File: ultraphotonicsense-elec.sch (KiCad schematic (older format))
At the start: 11 parts, among them J1 Conn_SWD_UART, U1 TXB0108PW, U2 74HC164

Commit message: Improved tracks spacing
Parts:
- J1: footprint Connector_JST:JST_PH_B8B-PH-K_1x08_P2.00mm_Vertical -> Connector_JST:JST_XH_B08B-XH-A_1x08_P2.50mm_Vertical
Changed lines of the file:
@@
 F 0 "J1" V 3117 2646 50  0000 C CNN
 F 1 "Conn_SWD_UART" V 3026 2646 50  0000 C CNN
-F 2 "Connector_JST:JST_PH_B8B-PH-K_1x08_P2.00mm_Vertical" H 2900 2700 50  0001 C CNN
+F 2 "Connector_JST:JST_XH_B08B-XH-A_1x08_P2.50mm_Vertical" H 2900 2700 50  0001 C CNN
 F 3 "~" H 2900 2700 50  0001 C CNN
 	1    2900 2700

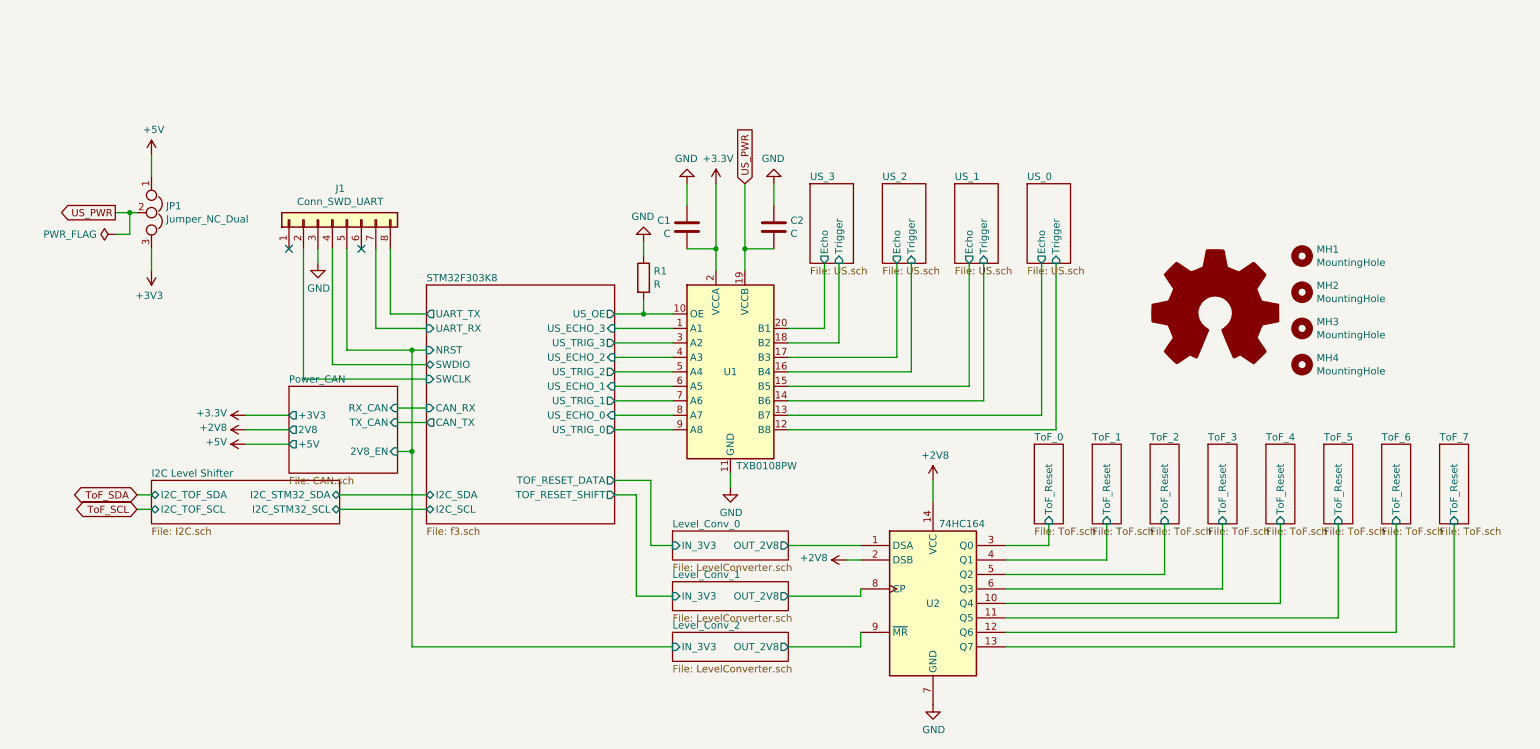
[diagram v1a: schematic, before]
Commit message: Corrected, routing redone
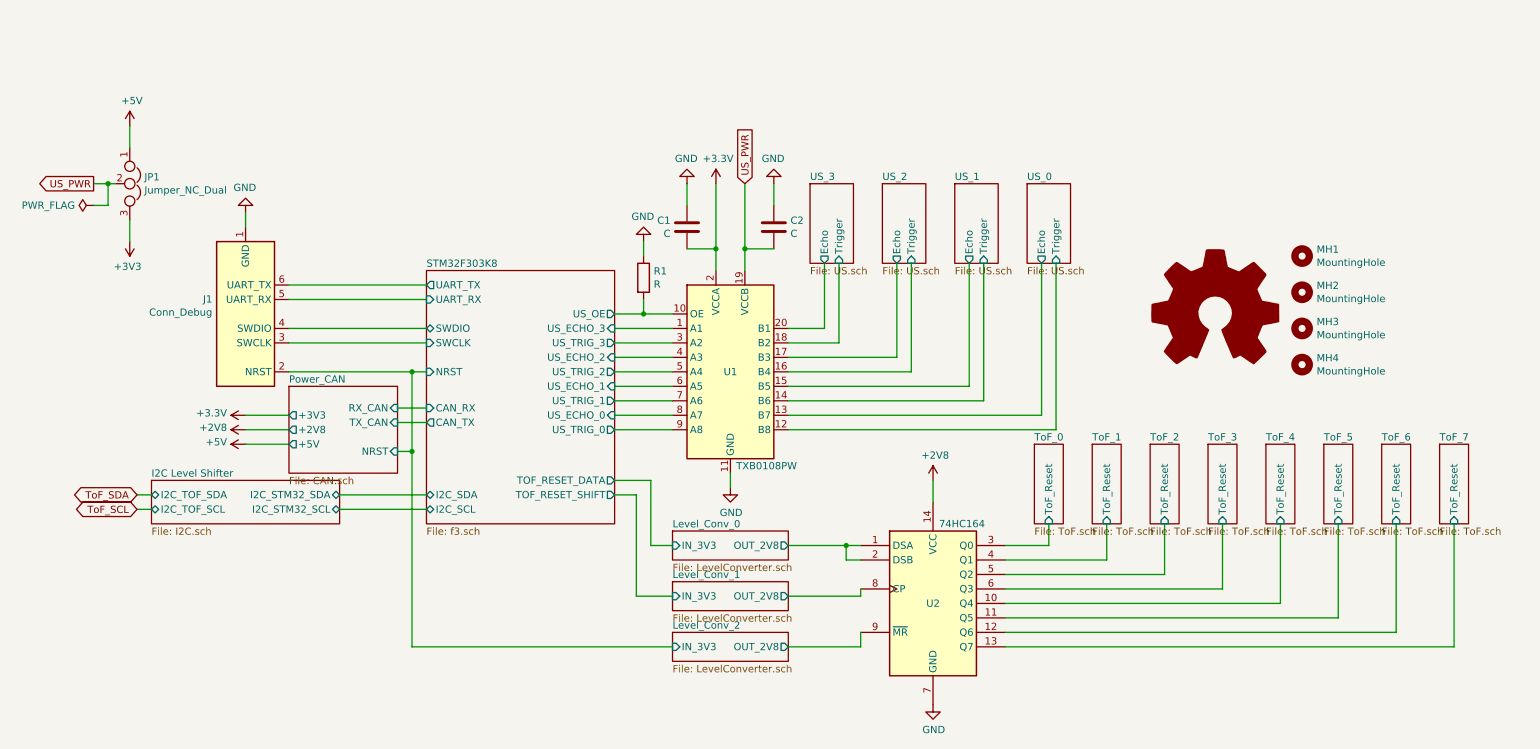
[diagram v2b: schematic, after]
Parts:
- removed J1: Conn_SWD_UART, Connector_JST:JST_XH_B08B-XH-A_1x08_P2.50mm_Vertical, symbol Connector_Generic:Conn_01x08
- added J1: Conn_Debug, Connector_JST:JST_PH_B6B-PH-K_1x06_P2.00mm_Vertical, symbol PhoenixRobotik:Conn_Debug
- U2: RS (none) -> 671-1753
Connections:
- net +2V8: no longer U2.2 (DSB)
- net GND: now also J1.1 (GND)
- net Level_Conv_0/OUT_2V8: now also U2.2 (DSB)
- net Level_Conv_2/IN_3V3: now also J1.2 (NRST)
- net STM32F303K8/SWCLK: now also J1.3 (SWCLK)
- net STM32F303K8/SWDIO: now also J1.4 (SWDIO)
- net STM32F303K8/UART_RX: now also J1.5 (UART_RX)
- net STM32F303K8/UART_TX: now also J1.6 (UART_TX)
- no-connect marks 2 -> 0
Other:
- moved on the sheet: JP1
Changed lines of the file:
@@
 F2 "RX_CAN" I R 3350 4000 50
 F3 "TX_CAN" I R 3350 4100 50
-F4 "2V8_EN" I R 3350 4300 50
-F5 "2V8" O L 2600 4150 50
-F6 "+3V3" O L 2600 4050 50
-F7 "+5V" O L 2600 4250 50
+F5 "+3V3" O L 2600 4050 50
+F6 "+5V" O L 2600 4250 50
+F7 "NRST" I R 3350 4300 50
+F8 "+2V8" O L 2600 4150 50
 $EndSheet
 $Sheet
@@
 $EndComp
 $Comp
-L Connector_Generic:Conn_01x08 J1
-U 1 1 5BBC14EB
-P 2900 2700
-F 0 "J1" V 3117 2646 50  0000 C CNN
-F 1 "Conn_SWD_UART" V 3026 2646 50  0000 C CNN
-F 2 "Connector_JST:JST_XH_B08B-XH-A_1x08_P2.50mm_Vertical" H 2900 2700 50  0001 C CNN
-F 3 "~" H 2900 2700 50  0001 C CNN
-	1    2900 2700
-	0    -1   -1   0
-$EndComp
-Wire Wire Line
-	3300 2900 3300 3350
-Wire Wire Line
-	3300 3350 3550 3350
-Wire Wire Line
-	3200 2900 3200 3450
-Wire Wire Line
-	3200 3450 3550 3450
-NoConn ~ 3100 2900
-Wire Wire Line
-	3000 2900 3000 3600
-Wire Wire Line
-	3000 3600 3450 3600
-Wire Wire Line
-	2900 2900 2900 3700
-Wire Wire Line
-	2900 3700 3550 3700
-$Comp
 L power:GND #PWR07
 U 1 1 5BBC1836
-P 2800 3000
-F 0 "#PWR07" H 2800 2750 50  0001 C CNN
-F 1 "GND" H 2805 2827 50  0000 C CNN
-F 2 "" H 2800 3000 50  0001 C CNN
-F 3 "" H 2800 3000 50  0001 C CNN
-	1    2800 3000
-	1    0    0    -1
-$EndComp
-Wire Wire Line
-	2800 2900 2800 3000
-Wire Wire Line
-	2700 2900 2700 3800
-Wire Wire Line
-	2700 3800 3550 3800
+P 2300 2650
+F 0 "#PWR07" H 2300 2400 50  0001 C CNN
+F 1 "GND" H 2305 2477 50  0000 C CNN
+F 2 "" H 2300 2650 50  0001 C CNN
+F 3 "" H 2300 2650 50  0001 C CNN
+	1    2300 2650
+	-1   0    0    1
+$EndComp
 Wire Wire Line
 	3350 4000 3550 4000
@@
 Wire Wire Line
 	10650 5650 10650 4800
-Wire Wire Line
-	3450 3600 3450 4300
-Wire Wire Line
-	3450 4300 3350 4300
-Connection ~ 3450 3600
-Wire Wire Line
-	3450 3600 3550 3600
 $Comp
 L PhoenixRobotik:74HC164 U2
@@
 F 2 "Package_SO:SOIC-14_3.9x8.7mm_P1.27mm" H 7050 5350 50  0001 C CNN
 F 3 "https://assets.nexperia.com/documents/data-sheet/74HC_HCT164.pdf" H 7050 5350 50  0001 C CNN
+F 4 "671-1753" H 0   0   50  0001 C CNN "RS"
 	1    7050 5350
 	1    0    0    -1
@@
 Wire Wire Line
 	7050 4500 7050 4650
-$Comp
-L power:+2V8 #PWR013
-U 1 1 5BBFB7FF
-P 6450 5050
-F 0 "#PWR013" H 6450 4900 50  0001 C CNN
-F 1 "+2V8" V 6465 5178 50  0000 L CNN
-F 2 "" H 6450 5050 50  0001 C CNN
-F 3 "" H 6450 5050 50  0001 C CNN
-	1    6450 5050
-	0    -1   -1   0
-$EndComp
 Wire Wire Line
 	6450 5050 6550 5050
 $Sheet
-S 3550 3150 1300 1650
+S 3550 3050 1300 1750
 U 5BBD3D7F
 F0 "STM32F303K8" 50
 F1 "f3.sch" 50
-F2 "UART_TX" O L 3550 3350 50
-F3 "UART_RX" I L 3550 3450 50
+F2 "UART_TX" O L 3550 3150 50
+F3 "UART_RX" I L 3550 3250 50
 F4 "CAN_RX" I L 3550 4000 50
 F5 "CAN_TX" O L 3550 4100 50
-F6 "SWDIO" B L 3550 3700 50
-F7 "SWCLK" I L 3550 3800 50
+F6 "SWDIO" B L 3550 3450 50
+F7 "SWCLK" I L 3550 3550 50
 F8 "I2C_SCL" B L 3550 4700 50
 F9 "I2C_SDA" B L 3550 4600 50
-F10 "NRST" I L 3550 3600 50
+F10 "NRST" I L 3550 3750 50
 F11 "TOF_RESET_DATA" O R 4850 4500 50
 F12 "TOF_RESET_SHIFT" O R 4850 4600 50
@@
 $EndSheet
 Wire Wire Line
-	6050 4950 6550 4950
+	6050 4950 6450 4950
 Wire Wire Line
 	5550 2900 5550 3050
@@
 L Device:Jumper_NC_Dual JP1
 U 1 1 5BC62830
-P 1650 2650
-F 0 "JP1" V 1604 2751 50  0000 L CNN
-F 1 "Jumper_NC_Dual" V 1695 2751 50  0000 L CNN
-F 2 "Connector_PinHeader_2.54mm:PinHeader_1x03_P2.54mm_Vertical" H 1650 2650 50  0001 C CNN
-F 3 "~" H 1650 2650 50  0001 C CNN
-	1    1650 2650
+P 1500 2450
+F 0 "JP1" V 1454 2551 50  0000 L CNN
+F 1 "Jumper_NC_Dual" V 1545 2551 50  0000 L CNN
+F 2 "Connector_PinHeader_2.54mm:PinHeader_1x03_P2.54mm_Vertical" H 1500 2450 50  0001 C CNN
+F 3 "~" H 1500 2450 50  0001 C CNN
+	1    1500 2450
 	0    1    1    0
 $EndComp
-Text GLabel 1400 2650 0    50   Output ~ 0
+Text GLabel 1250 2450 0    50   Output ~ 0
 US_PWR
 Wire Wire Line
-	1400 2650 1500 2650
+	1250 2450 1350 2450
 $Comp
 L power:+5V #PWR01
 U 1 1 5BC6506A
-P 1650 2250
-F 0 "#PWR01" H 1650 2100 50  0001 C CNN
-F 1 "+5V" H 1665 2423 50  0000 C CNN
-F 2 "" H 1650 2250 50  0001 C CNN
-F 3 "" H 1650 2250 50  0001 C CNN
-	1    1650 2250
-	1    0    0    -1
-$EndComp
-Wire Wire Line
-	1650 2250 1650 2400
+P 1500 2050
+F 0 "#PWR01" H 1500 1900 50  0001 C CNN
+F 1 "+5V" H 1515 2223 50  0000 C CNN
+F 2 "" H 1500 2050 50  0001 C CNN
+F 3 "" H 1500 2050 50  0001 C CNN
+	1    1500 2050
+	1    0    0    -1
+$EndComp
+Wire Wire Line
+	1500 2050 1500 2200
 $Comp
 L power:+3V3 #PWR02
 U 1 1 5BC678E1
-P 1650 3050
-F 0 "#PWR02" H 1650 2900 50  0001 C CNN
-F 1 "+3V3" H 1665 3223 50  0000 C CNN
-F 2 "" H 1650 3050 50  0001 C CNN
-F 3 "" H 1650 3050 50  0001 C CNN
-	1    1650 3050
+P 1500 2850
+F 0 "#PWR02" H 1500 2700 50  0001 C CNN
+F 1 "+3V3" H 1515 3023 50  0000 C CNN
+F 2 "" H 1500 2850 50  0001 C CNN
+F 3 "" H 1500 2850 50  0001 C CNN
+	1    1500 2850
 	-1   0    0    1
 $EndComp
 Wire Wire Line
-	1650 2900 1650 3050
+	1500 2700 1500 2850
 $Comp
 L power:+3.3V #PWR010
@@
 L power:PWR_FLAG #FLG01
 U 1 1 5BC6A929
-P 1400 2800
-F 0 "#FLG01" H 1400 2875 50  0001 C CNN
-F 1 "PWR_FLAG" V 1400 2928 50  0000 L CNN
-F 2 "" H 1400 2800 50  0001 C CNN
-F 3 "~" H 1400 2800 50  0001 C CNN
-	1    1400 2800
+P 1250 2600
+F 0 "#FLG01" H 1250 2675 50  0001 C CNN
+F 1 "PWR_FLAG" V 1250 2728 50  0000 L CNN
+F 2 "" H 1250 2600 50  0001 C CNN
+F 3 "~" H 1250 2600 50  0001 C CNN
+	1    1250 2600
 	0    -1   -1   0
 $EndComp
 Wire Wire Line
-	1500 2650 1500 2800
-Wire Wire Line
-	1500 2800 1400 2800
-Connection ~ 1500 2650
-Wire Wire Line
-	1500 2650 1550 2650
+	1350 2450 1350 2600
+Wire Wire Line
+	1350 2600 1250 2600
+Connection ~ 1350 2450
+Wire Wire Line
+	1350 2450 1400 2450
 Wire Wire Line
 	5650 4450 5650 4550
@@
 	6800 3000 6800 3650
 Wire Wire Line
+	3450 5650 5250 5650
+Wire Wire Line
+	6050 5650 6550 5650
+Wire Wire Line
+	6550 5650 6550 5550
+Wire Wire Line
+	6550 5300 6550 5250
+Wire Wire Line
+	6050 5300 6550 5300
+Wire Wire Line
+	3350 4300 3450 4300
+Wire Wire Line
 	3450 4300 3450 5650
-Wire Wire Line
-	3450 5650 5250 5650
+$Comp
+L PhoenixRobotik:Conn_Debug J1
+U 1 1 5BD16E64
+P 2300 3350
+F 0 "J1" H 2530 3248 50  0000 L CNN
+F 1 "Conn_Debug" H 2530 3339 50  0000 L CNN
+F 2 "Connector_JST:JST_PH_B6B-PH-K_1x06_P2.00mm_Vertical" H 2700 2050 50  0001 C CNN
+F 3 "~" H 4500 3150 50  0001 C CNN
+	1    2300 3350
+	-1   0    0    1
+$EndComp
+Wire Wire Line
+	2300 2650 2300 2750
+Wire Wire Line
+	3550 3750 3450 3750
+Wire Wire Line
+	3450 3750 3450 4300
 Connection ~ 3450 4300
 Wire Wire Line
-	6050 5650 6550 5650
-Wire Wire Line
-	6550 5650 6550 5550
-Wire Wire Line
-	6550 5300 6550 5250
-Wire Wire Line
-	6050 5300 6550 5300
-NoConn ~ 2600 2900
+	2600 3750 3450 3750
+Connection ~ 3450 3750
+Wire Wire Line
+	2600 3550 3550 3550
+Wire Wire Line
+	2600 3450 3550 3450
+Wire Wire Line
+	2600 3250 3550 3250
+Wire Wire Line
+	2600 3150 3550 3150
+Wire Wire Line
+	6450 5050 6450 4950
+Connection ~ 6450 4950
+Wire Wire Line
+	6450 4950 6550 4950
 $EndSCHEMATC

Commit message: Added RS refs
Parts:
- J1: RS (none) -> 820-1447
- JP1: RS (none) -> 251-8092
- U1: RS (none) -> 709-9038
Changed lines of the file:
@@
 F2 "RX_CAN" I R 3350 4000 50
 F3 "TX_CAN" I R 3350 4100 50
-F5 "+3V3" O L 2600 4050 50
-F6 "+5V" O L 2600 4250 50
-F7 "NRST" I R 3350 4300 50
-F8 "+2V8" O L 2600 4150 50
+F4 "+3V3" O L 2600 4050 50
+F5 "+5V" O L 2600 4250 50
+F6 "NRST" I R 3350 4300 50
+F7 "+2V8" O L 2600 4150 50
 $EndSheet
 $Sheet
@@
 F 2 "Package_SO:TSSOP-20_4.4x6.5mm_P0.65mm" H 5650 3000 50  0001 C CNN
 F 3 "http://www.ti.com/lit/ds/symlink/txb0108.pdf" H 5650 3650 50  0001 C CNN
+F 4 "709-9038" H 0   0   50  0001 C CNN "RS"
 	1    5650 3750
 	1    0    0    -1
@@
 F 2 "Connector_PinHeader_2.54mm:PinHeader_1x03_P2.54mm_Vertical" H 1500 2450 50  0001 C CNN
 F 3 "~" H 1500 2450 50  0001 C CNN
+F 4 "251-8092" H 0   0   50  0001 C CNN "RS"
 	1    1500 2450
 	0    1    1    0
@@
 F 2 "Connector_JST:JST_PH_B6B-PH-K_1x06_P2.00mm_Vertical" H 2700 2050 50  0001 C CNN
 F 3 "~" H 4500 3150 50  0001 C CNN
+F 4 "820-1447" H 0   0   50  0001 C CNN "RS"
 	1    2300 3350
 	-1   0    0    1

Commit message: Improved text placement
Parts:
- J1: symbol PhoenixRobotik:Conn_Debug -> PhenixRobotik:Conn_Debug
- U1: symbol PhoenixRobotik:TXB0108PW -> PhenixRobotik:TXB0108PW
- U2: symbol PhoenixRobotik:74HC164 -> PhenixRobotik:74HC164
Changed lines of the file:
@@
 	10650 5650 10650 4800
 $Comp
-L PhoenixRobotik:74HC164 U2
+L PhenixRobotik:74HC164 U2
 U 1 1 5BBF77F3
 P 7050 5350
@@
 $EndSheet
 $Comp
-L PhoenixRobotik:TXB0108PW U1
+L PhenixRobotik:TXB0108PW U1
 U 1 1 5BC00788
 P 5650 3750
@@
 	3450 4300 3450 5650
 $Comp
-L PhoenixRobotik:Conn_Debug J1
+L PhenixRobotik:Conn_Debug J1
 U 1 1 5BD16E64
 P 2300 3350

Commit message: Added component values
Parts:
- C1, C2: value C -> 100n
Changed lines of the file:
@@
 EESchema Schematic File Version 4
-LIBS:ultraphotonicsense-elec-cache
 EELAYER 26 0
 EELAYER END
@@
 P 5350 2750
 F 0 "C1" H 5236 2704 50  0000 R CNN
-F 1 "C" H 5236 2795 50  0000 R CNN
+F 1 "100n" H 5236 2795 50  0000 R CNN
 F 2 "Capacitor_SMD:C_0805_2012Metric_Pad1.15x1.40mm_HandSolder" H 5388 2600 50  0001 C CNN
 F 3 "~" H 5350 2750 50  0001 C CNN
@@
 P 5950 2750
 F 0 "C2" H 6065 2796 50  0000 L CNN
-F 1 "C" H 6065 2705 50  0000 L CNN
+F 1 "100n" H 6065 2705 50  0000 L CNN
 F 2 "Capacitor_SMD:C_0805_2012Metric_Pad1.15x1.40mm_HandSolder" H 5988 2600 50  0001 C CNN
 F 3 "~" H 5950 2750 50  0001 C CNN

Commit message: Rename phoenix phenix. Connect mounting holes to gnd.
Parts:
- removed MH1, MH2, MH3, MH4: MountingHole, MountingHole:MountingHole_2.7mm_M2.5, symbol Mechanical:MountingHole
- added MH1, MH2, MH3, MH4: MountingHole_Pad, MountingHole:MountingHole_2.2mm_M2_Pad, symbol Mechanical:MountingHole_Pad
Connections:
- wire segments 94 -> 98
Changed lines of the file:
@@
 EESchema Schematic File Version 4
+LIBS:ultraphotonicsense-elec-cache
 EELAYER 26 0
 EELAYER END
@@
 F3 "Echo" O B 6300 3000 50
 $EndSheet
-$Comp
-L Graphic:Logo_Open_Hardware_Large #LOGO1
-U 1 1 5BBE6179
-P 9000 3350
-F 0 "#LOGO1" H 9000 3850 50  0001 C CNN
-F 1 "Logo_Open_Hardware_Large" H 9000 2950 50  0001 C CNN
-F 2 "" H 9000 3350 50  0001 C CNN
-F 3 "~" H 9000 3350 50  0001 C CNN
-	1    9000 3350
-	1    0    0    -1
-$EndComp
-$Comp
-L Mechanical:MountingHole MH1
-U 1 1 5BBE6263
-P 9600 2950
-F 0 "MH1" H 9700 2996 50  0000 L CNN
-F 1 "MountingHole" H 9700 2905 50  0000 L CNN
-F 2 "MountingHole:MountingHole_2.7mm_M2.5" H 9600 2950 50  0001 C CNN
-F 3 "~" H 9600 2950 50  0001 C CNN
-	1    9600 2950
-	1    0    0    -1
-$EndComp
-$Comp
-L Mechanical:MountingHole MH2
-U 1 1 5BBE62B0
-P 9600 3200
-F 0 "MH2" H 9700 3246 50  0000 L CNN
-F 1 "MountingHole" H 9700 3155 50  0000 L CNN
-F 2 "MountingHole:MountingHole_2.7mm_M2.5" H 9600 3200 50  0001 C CNN
-F 3 "~" H 9600 3200 50  0001 C CNN
-	1    9600 3200
-	1    0    0    -1
-$EndComp
-$Comp
-L Mechanical:MountingHole MH3
-U 1 1 5BBE62F0
-P 9600 3450
-F 0 "MH3" H 9700 3496 50  0000 L CNN
-F 1 "MountingHole" H 9700 3405 50  0000 L CNN
-F 2 "MountingHole:MountingHole_2.7mm_M2.5" H 9600 3450 50  0001 C CNN
-F 3 "~" H 9600 3450 50  0001 C CNN
-	1    9600 3450
-	1    0    0    -1
-$EndComp
-$Comp
-L Mechanical:MountingHole MH4
-U 1 1 5BBE6333
-P 9600 3700
-F 0 "MH4" H 9700 3746 50  0000 L CNN
-F 1 "MountingHole" H 9700 3655 50  0000 L CNN
-F 2 "MountingHole:MountingHole_2.7mm_M2.5" H 9600 3700 50  0001 C CNN
-F 3 "~" H 9600 3700 50  0001 C CNN
-	1    9600 3700
-	1    0    0    -1
-$EndComp
 $Sheet
 S 5250 5550 800  200
@@
 Wire Wire Line
 	6450 4950 6550 4950
+$Comp
+L Mechanical:MountingHole_Pad MH1
+U 1 1 5BE093BE
+P 9800 3050
+F 0 "MH1" V 9754 3200 50  0000 L CNN
+F 1 "MountingHole_Pad" V 9845 3200 50  0000 L CNN
+F 2 "MountingHole:MountingHole_2.2mm_M2_Pad" H 9800 3050 50  0001 C CNN
+F 3 "~" H 9800 3050 50  0001 C CNN
+	1    9800 3050
+	0    1    1    0
+$EndComp
+$Comp
+L Mechanical:MountingHole_Pad MH2
+U 1 1 5BE09443
+P 9800 3250
+F 0 "MH2" V 9754 3400 50  0000 L CNN
+F 1 "MountingHole_Pad" V 9845 3400 50  0000 L CNN
+F 2 "MountingHole:MountingHole_2.2mm_M2_Pad" H 9800 3250 50  0001 C CNN
+F 3 "~" H 9800 3250 50  0001 C CNN
+	1    9800 3250
+	0    1    1    0
+$EndComp
+$Comp
+L Mechanical:MountingHole_Pad MH3
+U 1 1 5BE0949E
+P 9800 3450
+F 0 "MH3" V 9754 3600 50  0000 L CNN
+F 1 "MountingHole_Pad" V 9845 3600 50  0000 L CNN
+F 2 "MountingHole:MountingHole_2.2mm_M2_Pad" H 9800 3450 50  0001 C CNN
+F 3 "~" H 9800 3450 50  0001 C CNN
+	1    9800 3450
+	0    1    1    0
+$EndComp
+$Comp
+L Mechanical:MountingHole_Pad MH4
+U 1 1 5BE08F84
+P 9800 3650
+F 0 "MH4" V 9754 3800 50  0000 L CNN
+F 1 "MountingHole_Pad" V 9845 3800 50  0000 L CNN
+F 2 "MountingHole:MountingHole_2.2mm_M2_Pad" H 9800 3650 50  0001 C CNN
+F 3 "~" H 9800 3650 50  0001 C CNN
+	1    9800 3650
+	0    1    1    0
+$EndComp
+Wire Wire Line
+	9700 3050 9700 3250
+Connection ~ 9700 3250
+Wire Wire Line
+	9700 3250 9700 3450
+Connection ~ 9700 3450
+Wire Wire Line
+	9700 3450 9700 3650
+Connection ~ 9700 3650
+Wire Wire Line
+	9700 3650 9700 3800
+$Comp
+L power:GND #PWR0102
+U 1 1 5BE0B99C
+P 9700 3800
+F 0 "#PWR0102" H 9700 3550 50  0001 C CNN
+F 1 "GND" H 9705 3627 50  0000 C CNN
+F 2 "" H 9700 3800 50  0001 C CNN
+F 3 "" H 9700 3800 50  0001 C CNN
+	1    9700 3800
+	1    0    0    -1
+$EndComp
+$Comp
+L Graphic:Logo_Open_Hardware_Small #LOGO1
+U 1 1 5BE0F32B
+P 9300 1850
+F 0 "#LOGO1" H 9300 2125 50  0001 C CNN
+F 1 "Logo_Open_Hardware_Small" H 9300 1625 50  0001 C CNN
+F 2 "PhenixRobotik:Logo_16,9mm" H 9300 1850 50  0001 C CNN
+F 3 "~" H 9300 1850 50  0001 C CNN
+	1    9300 1850
+	1    0    0    -1
+$EndComp
+$Comp
+L Graphic:Logo_Open_Hardware_Small #LOGO2
+U 1 1 5BE0F4FA
+P 9750 1850
+F 0 "#LOGO2" H 9750 2125 50  0001 C CNN
+F 1 "Logo_Open_Hardware_Small" H 9750 1625 50  0001 C CNN
+F 2 "Symbol:OSHW-Logo2_7.3x6mm_SilkScreen" H 9750 1850 50  0001 C CNN
+F 3 "~" H 9750 1850 50  0001 C CNN
+	1    9750 1850
+	1    0    0    -1
+$EndComp
+$Comp
+L Graphic:Logo_Open_Hardware_Small #LOGO3
+U 1 1 5BE0F601
+P 10200 1850
+F 0 "#LOGO3" H 10200 2125 50  0001 C CNN
+F 1 "Logo_Open_Hardware_Small" H 10200 1625 50  0001 C CNN
+F 2 "Symbol:KiCad-Logo_6mm_SilkScreen" H 10200 1850 50  0001 C CNN
+F 3 "~" H 10200 1850 50  0001 C CNN
+	1    10200 1850
+	1    0    0    -1
+$EndComp
 $EndSCHEMATC

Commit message: update from schema
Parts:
- added LOGO1: Logo_Open_Hardware_Small, PhenixRobotik:Logo_16,9mm, symbol Graphic:Logo_Open_Hardware_Small
- added LOGO2: Logo_Open_Hardware_Small, Symbol:OSHW-Logo2_7.3x6mm_SilkScreen, symbol Graphic:Logo_Open_Hardware_Small
- added LOGO3: Logo_Open_Hardware_Small, Symbol:KiCad-Logo_6mm_SilkScreen, symbol Graphic:Logo_Open_Hardware_Small
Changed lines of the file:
@@
 $EndComp
 $Comp
-L Graphic:Logo_Open_Hardware_Small #LOGO1
+L Graphic:Logo_Open_Hardware_Small LOGO1
 U 1 1 5BE0F32B
 P 9300 1850
-F 0 "#LOGO1" H 9300 2125 50  0001 C CNN
+F 0 "LOGO1" H 9300 2125 50  0001 C CNN
 F 1 "Logo_Open_Hardware_Small" H 9300 1625 50  0001 C CNN
 F 2 "PhenixRobotik:Logo_16,9mm" H 9300 1850 50  0001 C CNN
@@
 $EndComp
 $Comp
-L Graphic:Logo_Open_Hardware_Small #LOGO2
+L Graphic:Logo_Open_Hardware_Small LOGO2
 U 1 1 5BE0F4FA
 P 9750 1850
-F 0 "#LOGO2" H 9750 2125 50  0001 C CNN
+F 0 "LOGO2" H 9750 2125 50  0001 C CNN
 F 1 "Logo_Open_Hardware_Small" H 9750 1625 50  0001 C CNN
 F 2 "Symbol:OSHW-Logo2_7.3x6mm_SilkScreen" H 9750 1850 50  0001 C CNN
@@
 $EndComp
 $Comp
-L Graphic:Logo_Open_Hardware_Small #LOGO3
+L Graphic:Logo_Open_Hardware_Small LOGO3
 U 1 1 5BE0F601
 P 10200 1850
-F 0 "#LOGO3" H 10200 2125 50  0001 C CNN
+F 0 "LOGO3" H 10200 2125 50  0001 C CNN
 F 1 "Logo_Open_Hardware_Small" H 10200 1625 50  0001 C CNN
 F 2 "Symbol:KiCad-Logo_6mm_SilkScreen" H 10200 1850 50  0001 C CNN

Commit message: Added resistors values
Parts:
- R1: value R -> pull
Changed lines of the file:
@@
 P 5050 3100
 F 0 "R1" H 5120 3146 50  0000 L CNN
-F 1 "R" H 5120 3055 50  0000 L CNN
+F 1 "pull" H 5120 3055 50  0000 L CNN
 F 2 "Resistor_SMD:R_0805_2012Metric_Pad1.15x1.40mm_HandSolder" V 4980 3100 50  0001 C CNN
 F 3 "~" H 5050 3100 50  0001 C CNN
